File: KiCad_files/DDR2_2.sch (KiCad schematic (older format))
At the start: 13 parts, among them J11 AS4C128M16D2A

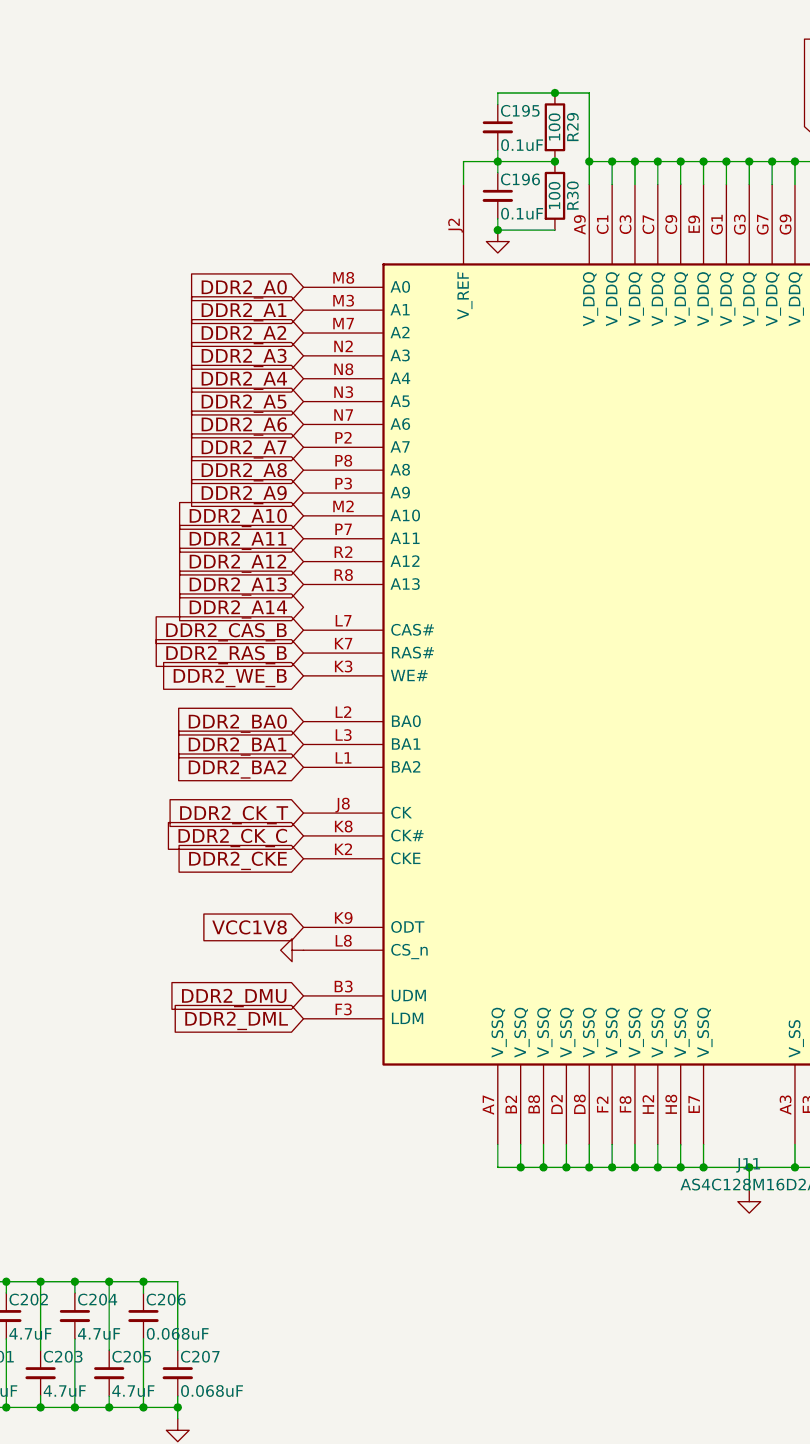
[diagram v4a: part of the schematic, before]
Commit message: More caps and added lots of test points
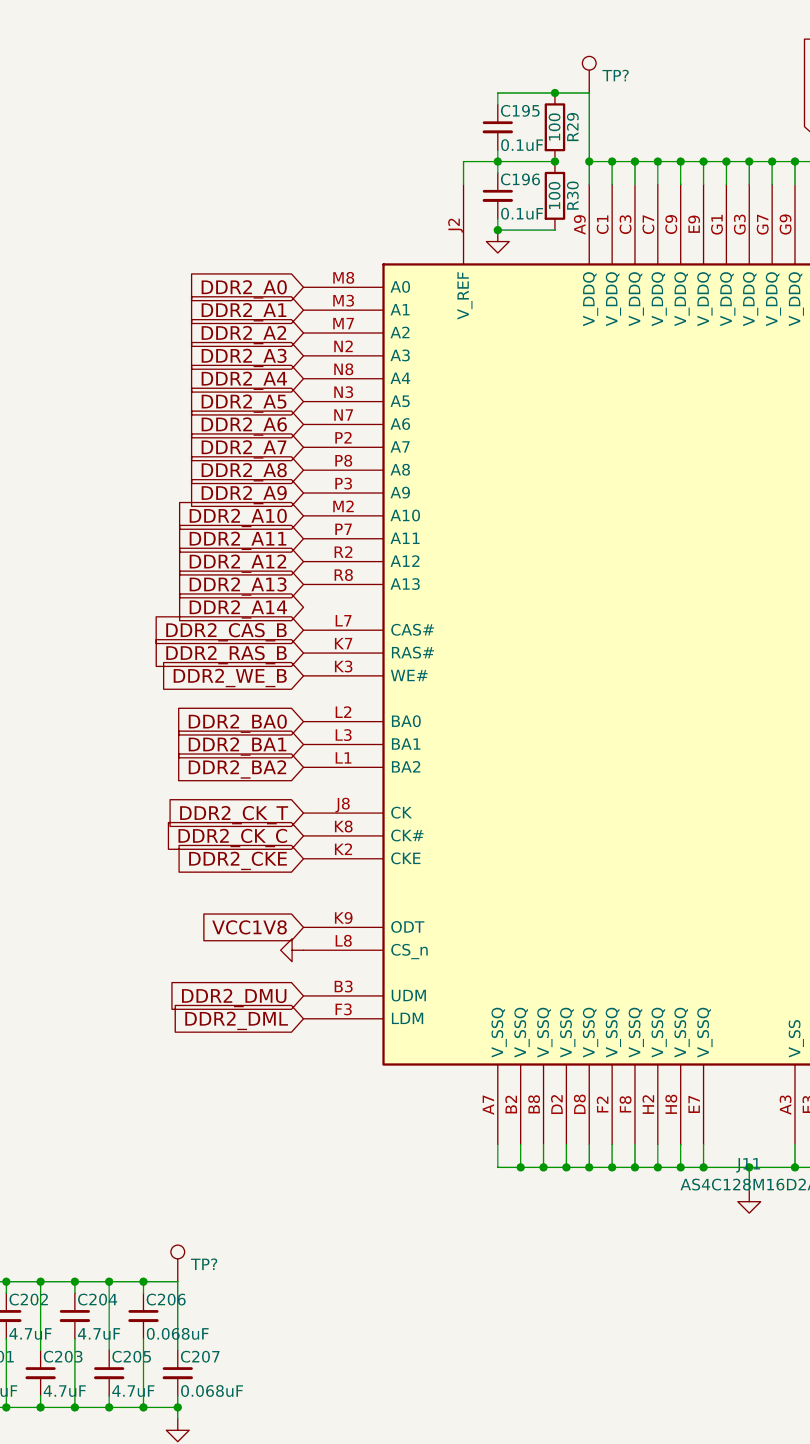
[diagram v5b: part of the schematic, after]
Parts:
- added TP? (x2): TestPoint, symbol Connector:TestPoint
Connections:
- net VCC1V8: now also TP?.1, TP?.1
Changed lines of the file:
@@
+	1    0    0    -1
+$EndComp
+$Comp
+L Connector:TestPoint TP?
+U 1 1 5CEA18FD
+P 5200 1350
+F 0 "TP?" H 5258 1424 50  0000 L CNN
+F 1 "TestPoint" H 5258 1379 50  0001 L CNN
+F 2 "" H 5400 1350 50  0001 C CNN
+F 3 "~" H 5400 1350 50  0001 C CNN
+	1    5200 1350
+	1    0    0    -1
+$EndComp
+$Comp
+L Connector:TestPoint TP?
+U 1 1 5CEA51A5
+P 3400 6550
+F 0 "TP?" H 3458 6624 50  0000 L CNN
+F 1 "TestPoint" H 3458 6579 50  0001 L CNN
+F 2 "" H 3600 6550 50  0001 C CNN
+F 3 "~" H 3600 6550 50  0001 C CNN
+	1    3400 6550
 	1    0    0    -1
 $EndComp

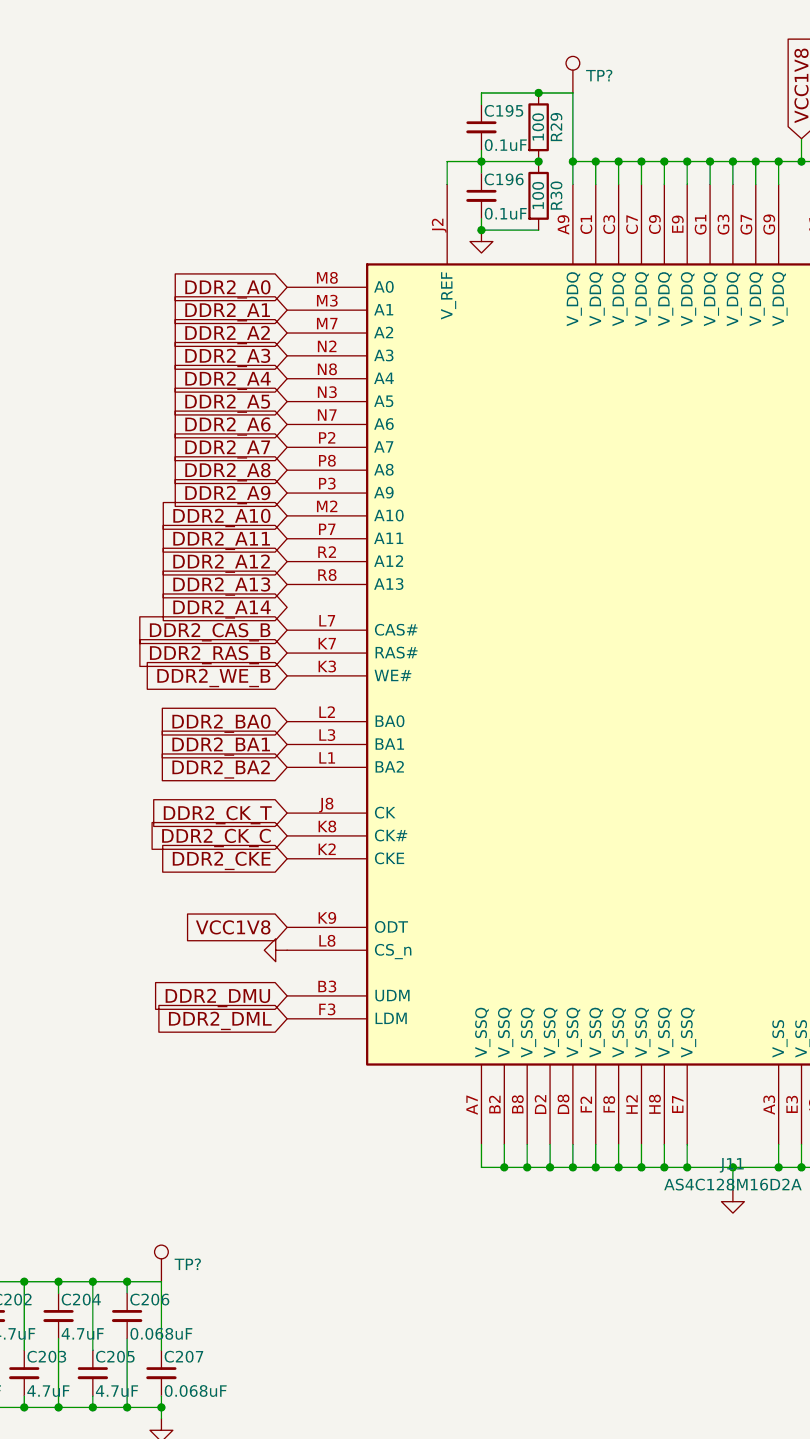
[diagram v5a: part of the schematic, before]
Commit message: Annotations and proper connections
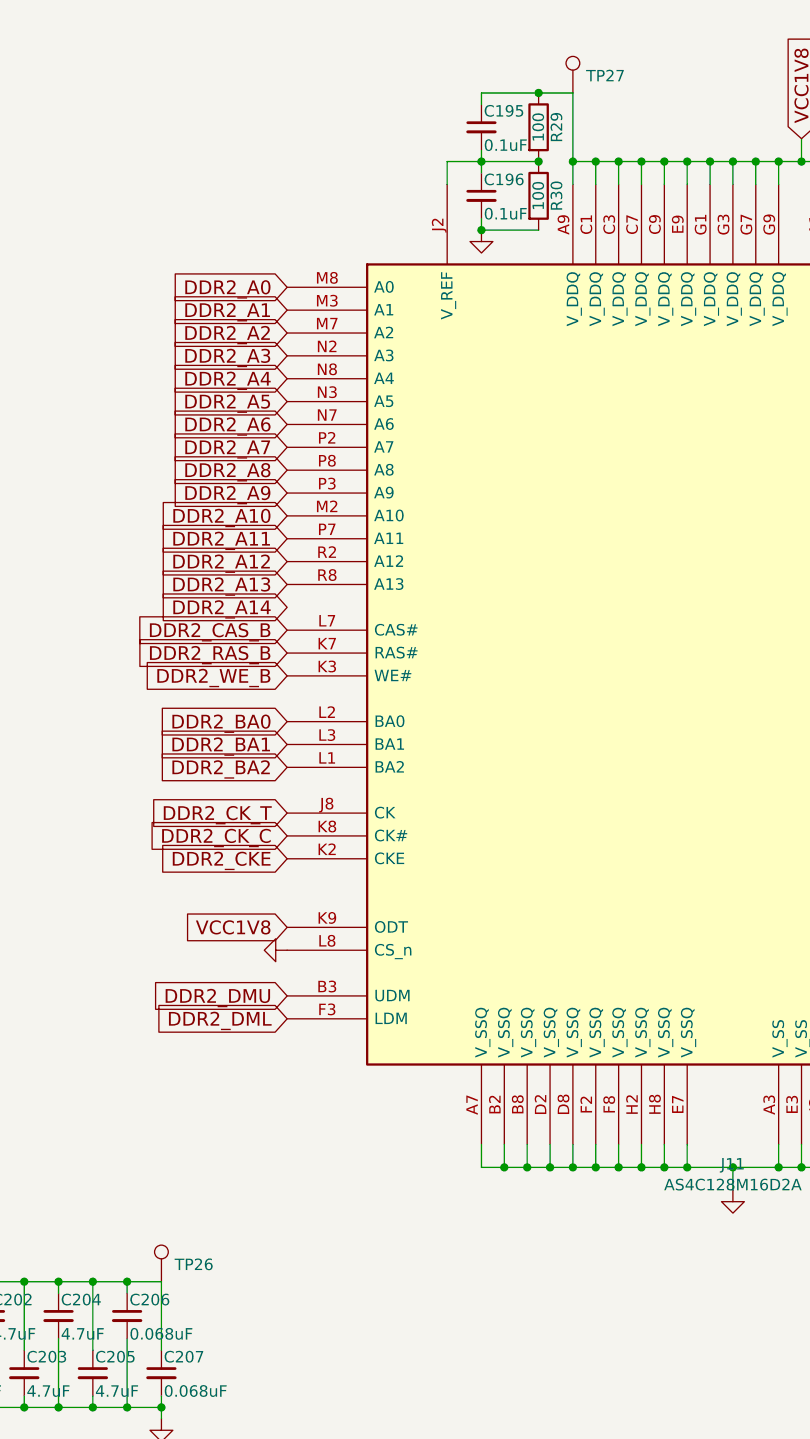
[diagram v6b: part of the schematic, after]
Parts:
- gave numbers to parts that had none: 2
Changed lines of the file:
@@
 U 1 1 5CEA18FD
 P 5200 1350
-F 0 "TP?" H 5258 1424 50  0000 L CNN
+AR Path="/5BFDDAF0/5CEA18FD" Ref="TP?"  Part="1"
+AR Path="/5C14AAFF/5CEA18FD" Ref="TP27"  Part="1"
+F 0 "TP27" H 5258 1424 50  0000 L CNN
 F 1 "TestPoint" H 5258 1379 50  0001 L CNN
 F 2 "" H 5400 1350 50  0001 C CNN
@@
 U 1 1 5CEA51A5
 P 3400 6550
-F 0 "TP?" H 3458 6624 50  0000 L CNN
+AR Path="/5BFDDAF0/5CEA51A5" Ref="TP?"  Part="1"
+AR Path="/5C14AAFF/5CEA51A5" Ref="TP26"  Part="1"
+F 0 "TP26" H 3458 6624 50  0000 L CNN
 F 1 "TestPoint" H 3458 6579 50  0001 L CNN
 F 2 "" H 3600 6550 50  0001 C CNN
